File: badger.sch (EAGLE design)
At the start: 44 parts, among them Q1 MOSFET-NCHANNEL2N7002PW, U1 NCP1402

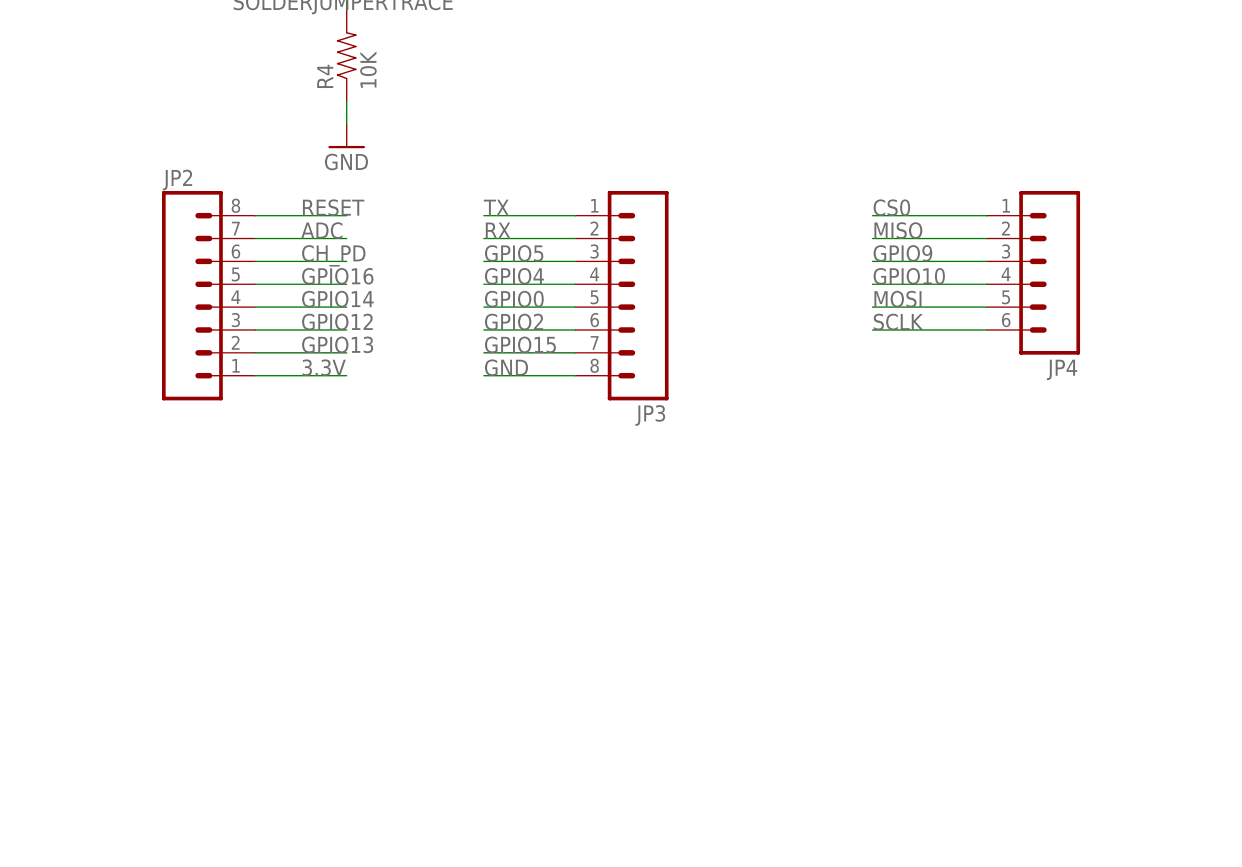
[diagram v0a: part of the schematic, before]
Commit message: Fix #3
All headers now locking
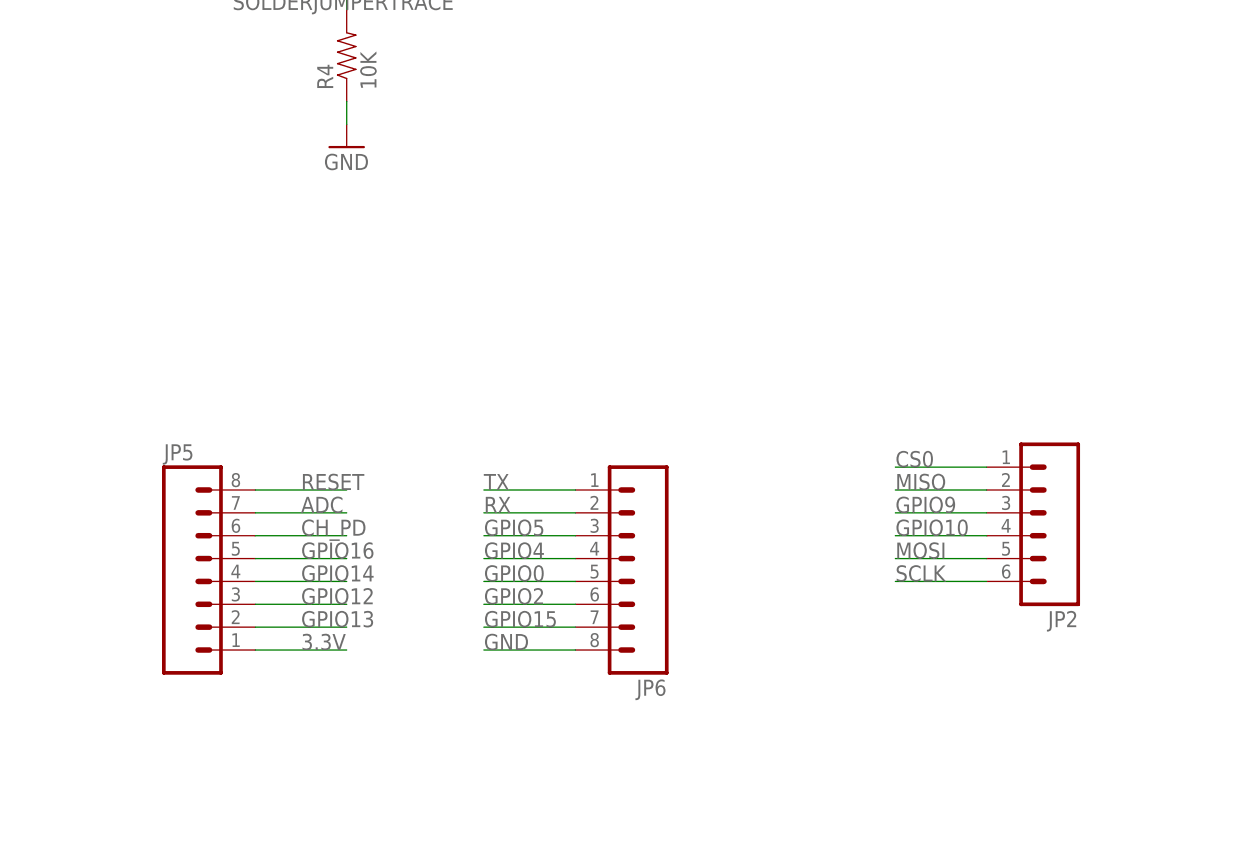
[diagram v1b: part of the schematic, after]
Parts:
- removed JP3: (no value), SparkFun-Connectors:M08
- removed JP4: (no value), SparkFun-Connectors:M06SILK_FEMALE_PTH
- added JP5, JP6: (no value), SparkFun-Connectors:M08LOCK
- JP2: device SparkFun-Connectors:M08 -> SparkFun-Connectors:M06LOCK
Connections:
- net 3.3V: now also JP5.1; no longer JP2.1
- net ADC: now also JP5.7; no longer JP2.7
- net CH_PD: now also JP5.6; no longer JP2.6
- net CS0: now also JP2.1; no longer JP4.1
- net GND: now also JP6.8; no longer JP3.8
- net GPIO0: now also JP6.5; no longer JP3.5
- net GPIO10: now also JP2.4; no longer JP4.4
- net GPIO12: now also JP5.3; no longer JP2.3
- net GPIO13: now also JP5.2; no longer JP2.2
- net GPIO14: now also JP5.4; no longer JP2.4
- net GPIO15: now also JP6.7; no longer JP3.7
- net GPIO16: now also JP5.5; no longer JP2.5
- net GPIO2: now also JP6.6; no longer JP3.6
- net GPIO4: now also JP6.4; no longer JP3.4
- net GPIO5: now also JP6.3; no longer JP3.3
- net GPIO9: now also JP2.3; no longer JP4.3
- net MISO: now also JP2.2; no longer JP4.2
- net MOSI: now also JP2.5; no longer JP4.5
- net RESET: now also JP5.8; no longer JP2.8
- net RX: now also JP6.2; no longer JP3.2
- net SCLK: now also JP2.6; no longer JP4.6
- net TX: now also JP6.1; no longer JP3.1

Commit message: as sent to oshpark for proto
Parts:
- added D7: 250mA/100V, SparkFun-DiscreteSemi:DIODEBAS16
- added LOGO1: OSHW-LOGOL-COPPER, SparkFun-Aesthetics:OSHW-LOGOL-COPPER
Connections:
- net GND: now also D7.A
- net N$18: now also D7.C
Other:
- moved on the sheet: Q1
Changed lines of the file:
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@@
 <part name="JP6" library="SparkFun-Connectors" deviceset="M08" device="LOCK"/>
 <part name="JP2" library="SparkFun-Connectors" deviceset="M06" device="LOCK"/>
+<part name="GND16" library="SparkFun" deviceset="GND" device=""/>
+<part name="D7" library="SparkFun-DiscreteSemi" deviceset="DIODE" device="BAS16" value="250mA/100V"/>
+<part name="LOGO1" library="SparkFun-Aesthetics" deviceset="OSHW-LOGO" device="L-COPPER"/>
 </parts>
 <sheets>
@@
 <attribute name="VALUE" x="-84.455" y="5.08" size="1.778" layer="96" rot="R90"/>
 </instance>
-<instance part="Q1" gate="G$1" x="-83.82" y="48.26" rot="R180"/>
-<instance part="GND14" gate="1" x="-83.82" y="35.56"/>
+<instance part="Q1" gate="G$1" x="-83.82" y="43.18" rot="R180"/>
+<instance part="GND14" gate="1" x="-83.82" y="30.48"/>
 <instance part="U$3" gate="G$1" x="-83.82" y="60.96" rot="R90"/>
 <instance part="VIN" gate="G$1" x="-119.38" y="-20.32"/>
@@
 <instance part="JP6" gate="G$1" x="139.7" y="-40.64" rot="R180"/>
 <instance part="JP2" gate="G$1" x="185.42" y="-35.56" rot="R180"/>
+<instance part="GND16" gate="1" x="5.08" y="33.02"/>
+<instance part="D7" gate="G$1" x="-97.79" y="43.18" rot="R90"/>
+<instance part="LOGO1" gate="G$1" x="-22.86" y="-30.48"/>
 </instances>
 <busses>
@@
 </segment>
 <segment>
-<wire x1="-12.7" y1="38.1" x2="-25.4" y2="38.1" width="0.1524" layer="91"/>
 <label x="-17.78" y="38.1" size="1.778" layer="95"/>
+<pinref part="GND16" gate="1" pin="GND"/>
+<wire x1="-25.4" y1="38.1" x2="5.08" y2="38.1" width="0.1524" layer="91"/>
+<wire x1="5.08" y1="38.1" x2="5.08" y2="35.56" width="0.1524" layer="91"/>
 </segment>
 <segment>
@@
 <pinref part="Q1" gate="G$1" pin="D"/>
 <pinref part="GND14" gate="1" pin="GND"/>
-<wire x1="-83.82" y1="43.18" x2="-83.82" y2="38.1" width="0.1524" layer="91"/>
+<wire x1="-83.82" y1="38.1" x2="-83.82" y2="36.83" width="0.1524" layer="91"/>
+<pinref part="D7" gate="G$1" pin="A"/>
+<wire x1="-83.82" y1="36.83" x2="-83.82" y2="33.02" width="0.1524" layer="91"/>
+<wire x1="-97.79" y1="40.64" x2="-97.79" y2="36.83" width="0.1524" layer="91"/>
+<wire x1="-97.79" y1="36.83" x2="-83.82" y2="36.83" width="0.1524" layer="91"/>
+<junction x="-83.82" y="36.83"/>
 </segment>
 <segment>
@@
 <segment>
 <pinref part="Q1" gate="G$1" pin="G"/>
-<wire x1="-76.2" y1="48.26" x2="-68.58" y2="48.26" width="0.1524" layer="91"/>
-<label x="-73.66" y="48.26" size="1.778" layer="95"/>
+<wire x1="-76.2" y1="43.18" x2="-68.58" y2="43.18" width="0.1524" layer="91"/>
+<label x="-73.66" y="43.18" size="1.778" layer="95"/>
 </segment>
 <segment>
@@
 <pinref part="U$3" gate="G$1" pin="1"/>
 <pinref part="Q1" gate="G$1" pin="S"/>
-<wire x1="-83.82" y1="55.88" x2="-83.82" y2="53.34" width="0.1524" layer="91"/>
-</segment>
-</net>
+<wire x1="-83.82" y1="55.88" x2="-83.82" y2="52.07" width="0.1524" layer="91"/>
+<pinref part="D7" gate="G$1" pin="C"/>
+<wire x1="-83.82" y1="52.07" x2="-83.82" y2="48.26" width="0.1524" layer="91"/>
+<wire x1="-83.82" y1="52.07" x2="-97.79" y2="52.07" width="0.1524" layer="91"/>
+<wire x1="-97.79" y1="52.07" x2="-97.79" y2="45.72" width="0.1524" layer="91"/>
+<junction x="-83.82" y="52.07"/>
+</segment>
+</net>

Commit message: fix #8
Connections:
- net GND: now also JP1.GND
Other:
- moved on the sheet: JP1
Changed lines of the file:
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@@
 <instance part="S1" gate="G$1" x="119.38" y="91.44" rot="R90"/>
 <instance part="S2" gate="G$1" x="205.74" y="50.8" rot="R90"/>
-<instance part="JP1" gate="G$1" x="-30.48" y="30.48"/>
+<instance part="JP1" gate="G$1" x="-27.94" y="30.48"/>
 <instance part="SUPPLY4" gate="G$1" x="205.74" y="76.2"/>
 <instance part="GND1" gate="1" x="205.74" y="35.56"/>
@@
 <label x="-17.78" y="38.1" size="1.778" layer="95"/>
 <pinref part="GND16" gate="1" pin="GND"/>
-<wire x1="-25.4" y1="38.1" x2="5.08" y2="38.1" width="0.1524" layer="91"/>
+<wire x1="-22.86" y1="38.1" x2="5.08" y2="38.1" width="0.1524" layer="91"/>
 <wire x1="5.08" y1="38.1" x2="5.08" y2="35.56" width="0.1524" layer="91"/>
+<pinref part="JP1" gate="G$1" pin="GND"/>
 </segment>
 <segment>
@@
 <segment>
 <pinref part="JP1" gate="G$1" pin="DTR"/>
-<wire x1="-25.4" y1="25.4" x2="-12.7" y2="25.4" width="0.1524" layer="91"/>
+<wire x1="-22.86" y1="25.4" x2="-12.7" y2="25.4" width="0.1524" layer="91"/>
 <label x="-17.78" y="25.4" size="1.778" layer="95"/>
 </segment>
@@
 <segment>
 <pinref part="JP1" gate="G$1" pin="TXO"/>
-<wire x1="-25.4" y1="30.48" x2="-12.7" y2="30.48" width="0.1524" layer="91"/>
+<wire x1="-22.86" y1="30.48" x2="-12.7" y2="30.48" width="0.1524" layer="91"/>
 <label x="-17.78" y="30.48" size="1.778" layer="95"/>
 </segment>
@@
 <segment>
 <pinref part="JP1" gate="G$1" pin="RXI"/>
-<wire x1="-25.4" y1="27.94" x2="-12.7" y2="27.94" width="0.1524" layer="91"/>
+<wire x1="-22.86" y1="27.94" x2="-12.7" y2="27.94" width="0.1524" layer="91"/>
 <label x="-17.78" y="27.94" size="1.778" layer="95"/>
 </segment>
@@
 <segment>
 <pinref part="JP1" gate="G$1" pin="CTS"/>
-<wire x1="-25.4" y1="35.56" x2="-12.7" y2="35.56" width="0.1524" layer="91"/>
+<wire x1="-22.86" y1="35.56" x2="-12.7" y2="35.56" width="0.1524" layer="91"/>
 <label x="-17.78" y="35.56" size="1.778" layer="95"/>
 </segment>
@@
 <segment>
 <pinref part="JP1" gate="G$1" pin="VCC"/>
-<wire x1="-25.4" y1="33.02" x2="-12.7" y2="33.02" width="0.1524" layer="91"/>
+<wire x1="-22.86" y1="33.02" x2="-12.7" y2="33.02" width="0.1524" layer="91"/>
 <label x="-17.78" y="33.02" size="1.778" layer="95"/>
 </segment>

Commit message: unrouted fixes
speaker/pin collision
add source bitmaps to repo
bsides logo now hi-res
oshpark logo
harmonize (mostly) silk placement and size
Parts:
- Q1: value MOSFET-NCHANNEL2N7002PW -> 2N7002PW
- renumbered U$2 to S3
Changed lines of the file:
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@@
 <part name="U$1" library="badger" deviceset="BATTERY" device=""/>
 <part name="GND10" library="SparkFun" deviceset="GND" device=""/>
-<part name="U$2" library="badger" deviceset="SSSS810701" device=""/>
+<part name="S3" library="badger" deviceset="SSSS810701" device=""/>
 <part name="SUPPLY1" library="SparkFun-Aesthetics" deviceset="3.3V" device=""/>
 <part name="D5" library="Seeed-OPL-Diode" deviceset="DIP-LED-RGB-COMMON-ANODE(4P-D5MM)" device="" value="FZR50RGB00T-C"/>
@@
 <part name="CHEAPO-3" library="SparkFun-Retired" deviceset="SOLDERJUMPER_2WAY" device="T"/>
 <part name="CHEAPO-7" library="SparkFun-Retired" deviceset="SOLDERJUMPER_2WAY" device="T"/>
-<part name="Q1" library="SparkFun-DiscreteSemi" deviceset="MOSFET-NCHANNEL" device="2N7002PW"/>
+<part name="Q1" library="SparkFun-DiscreteSemi" deviceset="MOSFET-NCHANNEL" device="2N7002PW" value="2N7002PW"/>
 <part name="GND14" library="SparkFun" deviceset="GND" device=""/>
 <part name="U$3" library="adafruit" deviceset="PS603" device="SPK"/>
@@
 <instance part="U$1" gate="G$1" x="-50.8" y="76.2" rot="R270"/>
 <instance part="GND10" gate="1" x="-50.8" y="63.5"/>
-<instance part="U$2" gate="G$1" x="149.86" y="-5.08"/>
+<instance part="S3" gate="G$1" x="149.86" y="-5.08"/>
 <instance part="SUPPLY1" gate="G$1" x="27.94" y="0"/>
 <instance part="D5" gate="G$1" x="20.32" y="-20.32" rot="R270"/>
@@
 <pinref part="SUPPLY1" gate="G$1" pin="3.3V"/>
 <wire x1="27.94" y1="0" x2="27.94" y2="-2.54" width="0.1524" layer="91"/>
-<pinref part="U$2" gate="G$1" pin="P"/>
+<pinref part="S3" gate="G$1" pin="P"/>
 <wire x1="38.1" y1="-2.54" x2="27.94" y2="-2.54" width="0.1524" layer="91"/>
 <label x="33.02" y="-2.54" size="1.778" layer="95"/>
@@
 </segment>
 <segment>
-<pinref part="U$2" gate="G$1" pin="O"/>
+<pinref part="S3" gate="G$1" pin="O"/>
 <wire x1="45.72" y1="0" x2="60.96" y2="0" width="0.1524" layer="91"/>
 <label x="55.88" y="0" size="1.778" layer="95"/>
@@
 <net name="VFTDI" class="0">
 <segment>
-<pinref part="U$2" gate="G$1" pin="S"/>
+<pinref part="S3" gate="G$1" pin="S"/>
 <wire x1="45.72" y1="-5.08" x2="58.42" y2="-5.08" width="0.1524" layer="91"/>
 <label x="55.88" y="-5.08" size="1.778" layer="95"/>

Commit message: final(?) design? - rerouted - rgb led now with common gnd - rgb led now powered by vin with cheapo varient - new cam
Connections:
- net 3.3V: no longer D5.+
- net GND: now also D5.+; no longer CHEAPO-4.3, CHEAPO-5.3, CHEAPO-6.3
- net GPIO15: now also Q1.G
- net GPIO16: no longer Q1.G
- net VIN: now also CHEAPO-4.3, CHEAPO-5.3, CHEAPO-6.3
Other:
- note added: "symbol is backwards. Diodes do go other way"
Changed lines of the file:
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@@
 <part name="SUPPLY1" library="SparkFun-Aesthetics" deviceset="3.3V" device=""/>
 <part name="D5" library="Seeed-OPL-Diode" deviceset="DIP-LED-RGB-COMMON-ANODE(4P-D5MM)" device="" value="FZR50RGB00T-C"/>
-<part name="SUPPLY5" library="SparkFun-Aesthetics" deviceset="3.3V" device=""/>
 <part name="R7" library="SparkFun-Resistors" deviceset="RESISTOR" device="1206" value="100"/>
 <part name="R8" library="SparkFun-Resistors" deviceset="RESISTOR" device="1206" value="100"/>
@@
 <part name="CHEAPO-6" library="SparkFun-Retired" deviceset="SOLDERJUMPER_2WAY" device="T"/>
 <part name="GND11" library="SparkFun" deviceset="GND" device=""/>
-<part name="GND12" library="SparkFun" deviceset="GND" device=""/>
-<part name="GND13" library="SparkFun" deviceset="GND" device=""/>
 <part name="R10" library="SparkFun-Resistors" deviceset="RESISTOR-ARRAY" device="0603-ARV" value="100"/>
 <part name="D6" library="SparkFun-LED" deviceset="LED" device="-3MM-NO_SILK"/>
@@
 <sheet>
 <plain>
+<text x="30.48" y="-20.32" size="1.778" layer="91">symbol is backwards.  Diodes do go other way</text>
 </plain>
 <instances>
@@
 <instance part="SUPPLY1" gate="G$1" x="27.94" y="0"/>
 <instance part="D5" gate="G$1" x="20.32" y="-20.32" rot="R270"/>
-<instance part="SUPPLY5" gate="G$1" x="20.32" y="-10.16"/>
 <instance part="R7" gate="G$1" x="33.02" y="-35.56" rot="R90"/>
 <instance part="R8" gate="G$1" x="20.32" y="-35.56" rot="R90"/>
@@
 <attribute name="VALUE" x="5.715" y="-71.12" size="1.778" layer="96" rot="R270"/>
 </instance>
-<instance part="GND11" gate="1" x="0" y="-73.66"/>
-<instance part="GND12" gate="1" x="12.7" y="-60.96"/>
-<instance part="GND13" gate="1" x="25.4" y="-53.34"/>
+<instance part="GND11" gate="1" x="7.62" y="-15.24"/>
 <instance part="R10" gate="A" x="-76.2" y="-15.24" rot="R90"/>
 <instance part="R10" gate="B" x="-66.04" y="-15.24" rot="R90"/>
@@
 </segment>
 <segment>
-<pinref part="CHEAPO-6" gate="G$1" pin="3"/>
-<pinref part="GND11" gate="1" pin="GND"/>
-<wire x1="2.54" y1="-68.58" x2="0" y2="-68.58" width="0.1524" layer="91"/>
-<wire x1="0" y1="-68.58" x2="0" y2="-71.12" width="0.1524" layer="91"/>
-</segment>
-<segment>
-<pinref part="CHEAPO-5" gate="G$1" pin="3"/>
-<pinref part="GND12" gate="1" pin="GND"/>
-<wire x1="15.24" y1="-58.42" x2="12.7" y2="-58.42" width="0.1524" layer="91"/>
-</segment>
-<segment>
-<pinref part="CHEAPO-4" gate="G$1" pin="3"/>
-<pinref part="GND13" gate="1" pin="GND"/>
-<wire x1="27.94" y1="-50.8" x2="25.4" y2="-50.8" width="0.1524" layer="91"/>
-</segment>
-<segment>
 <pinref part="Q1" gate="G$1" pin="D"/>
 <pinref part="GND14" gate="1" pin="GND"/>
@@
 <label x="124.46" y="-50.8" size="1.778" layer="95"/>
 </segment>
+<segment>
+<pinref part="D5" gate="G$1" pin="+"/>
+<wire x1="20.32" y1="-15.24" x2="20.32" y2="-7.62" width="0.1524" layer="91"/>
+<pinref part="GND11" gate="1" pin="GND"/>
+<wire x1="20.32" y1="-7.62" x2="7.62" y2="-7.62" width="0.1524" layer="91"/>
+<wire x1="7.62" y1="-7.62" x2="7.62" y2="-12.7" width="0.1524" layer="91"/>
+</segment>
 </net>
 <net name="VIN" class="0">
@@
 <label x="-129.54" y="-20.32" size="1.778" layer="95"/>
 </segment>
+<segment>
+<pinref part="CHEAPO-6" gate="G$1" pin="3"/>
+<wire x1="2.54" y1="-68.58" x2="0" y2="-68.58" width="0.1524" layer="91"/>
+<label x="-5.08" y="-68.58" size="1.778" layer="95"/>
+</segment>
+<segment>
+<pinref part="CHEAPO-5" gate="G$1" pin="3"/>
+<wire x1="15.24" y1="-58.42" x2="12.7" y2="-58.42" width="0.1524" layer="91"/>
+<label x="10.16" y="-58.42" size="1.778" layer="95"/>
+</segment>
+<segment>
+<pinref part="CHEAPO-4" gate="G$1" pin="3"/>
+<wire x1="27.94" y1="-50.8" x2="25.4" y2="-50.8" width="0.1524" layer="91"/>
+<label x="22.86" y="-50.8" size="1.778" layer="95"/>
+</segment>
 </net>
 <net name="RESET" class="0">
@@
 </segment>
 <segment>
-<pinref part="SUPPLY5" gate="G$1" pin="3.3V"/>
-<pinref part="D5" gate="G$1" pin="+"/>
-<wire x1="20.32" y1="-10.16" x2="20.32" y2="-15.24" width="0.1524" layer="91"/>
-</segment>
-<segment>
 <pinref part="SUPPLY6" gate="G$1" pin="3.3V"/>
 <wire x1="-134.62" y1="-38.1" x2="-134.62" y2="-40.64" width="0.1524" layer="91"/>
@@
 </segment>
 <segment>
-<pinref part="Q1" gate="G$1" pin="G"/>
-<wire x1="-76.2" y1="43.18" x2="-68.58" y2="43.18" width="0.1524" layer="91"/>
-<label x="-73.66" y="43.18" size="1.778" layer="95"/>
-</segment>
-<segment>
 <pinref part="JP5" gate="G$1" pin="5"/>
 <wire x1="99.06" y1="-40.64" x2="109.22" y2="-40.64" width="0.1524" layer="91"/>
@@
 <label x="124.46" y="-48.26" size="1.778" layer="95"/>
 </segment>
-</net>
+<segment>
+<pinref part="Q1" gate="G$1" pin="G"/>
+<wire x1="-76.2" y1="43.18" x2="-63.5" y2="43.18" width="0.1524" layer="91"/>
+<label x="-71.12" y="43.18" size="1.778" layer="95"/>
+</segment>
+</net>
